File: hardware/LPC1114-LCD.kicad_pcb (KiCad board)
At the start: 2 copper layers, 80 x 76 mm, 58 parts, among them J1 USB_B_Micro, J2 SWD, J3 UART, Q1 BC337, Q2 BC337, SW1 MODE/ISP, SW2 UP, SW3 DOWN, SW4 OK, SW5 RESET, U1 LPC1114FN28/102, U2 MCP1700-3302E/TO, U3 CH340C, U4 DS3231MZ+, Y1 12MHz

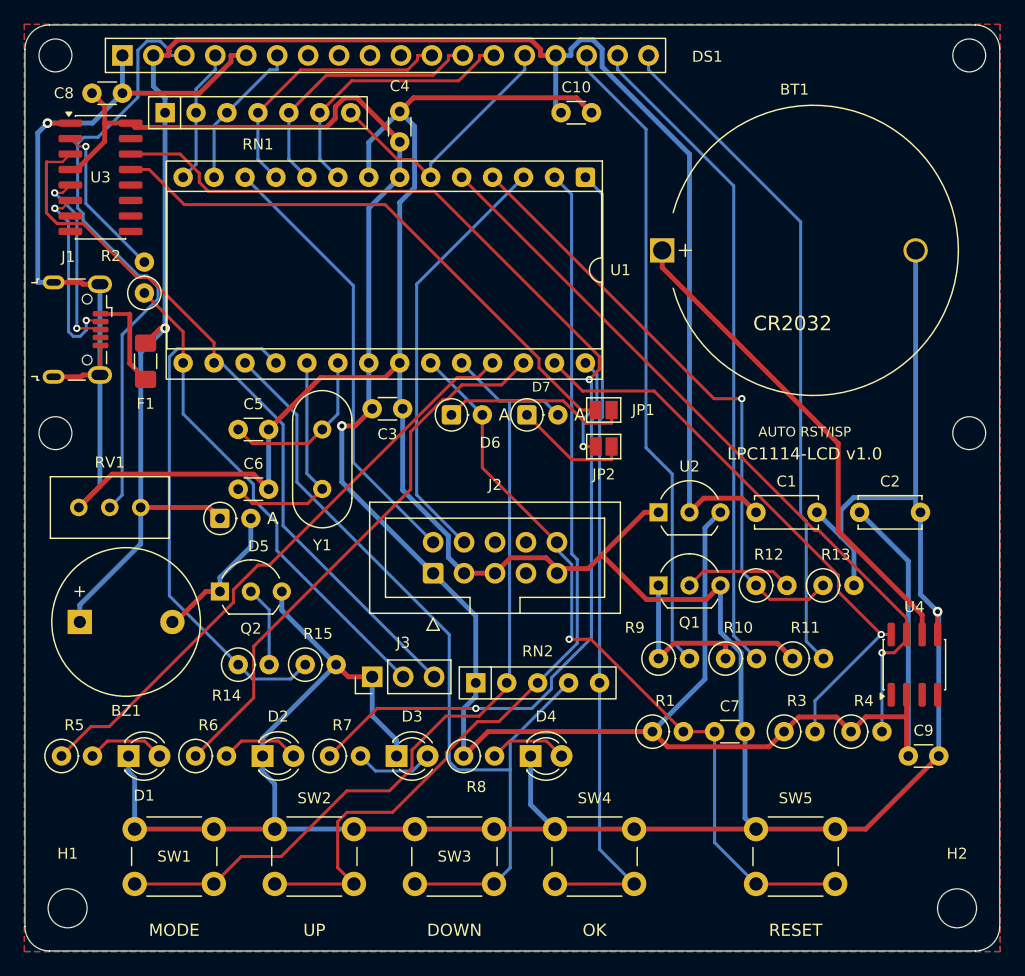
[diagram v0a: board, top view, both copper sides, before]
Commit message: Hardware v1.1: JLCPCB PCBA with Basic parts, Pomodoro timer, 80x52 mm
- Main use is now a Pomodoro timer: RTC (DS3231M) and CR2032 removed,
  timekeeping from the 12 MHz crystal; PTC fuse removed
- SMD redesign for JLCPCB assembly: 0603/0805 passives and LEDs,
  XC6206 LDO, SS8050, B5819W, 3225 crystal, TS-1187A buttons (all Basic);
  CH340C and micro USB are the only Extended parts
- User-soldered: LPC1114 (+socket), LCD, 10k multiturn trimmer,
  TDK PS1420P02CT piezo buzzer, USBLC6-2SC6, J2 (1x7 SWD+I2C) and
  J3 (1x3 UART) pads
- PCB reduced from 80x76 to 80x52 mm; ERC/DRC clean, parity OK, fully routed
- JLCPCB BOM + CPL and hand-solder list generated by export_fab.ps1
- Enclosure updated: 92.8x64.8x31.4 mm, longer button stems, LED light pipes
- Docs: schematic review for JLCPCB, design notes, README, board.h

Co-Authored-By: Claude Opus 5.5 <noreply@anthropic.com>
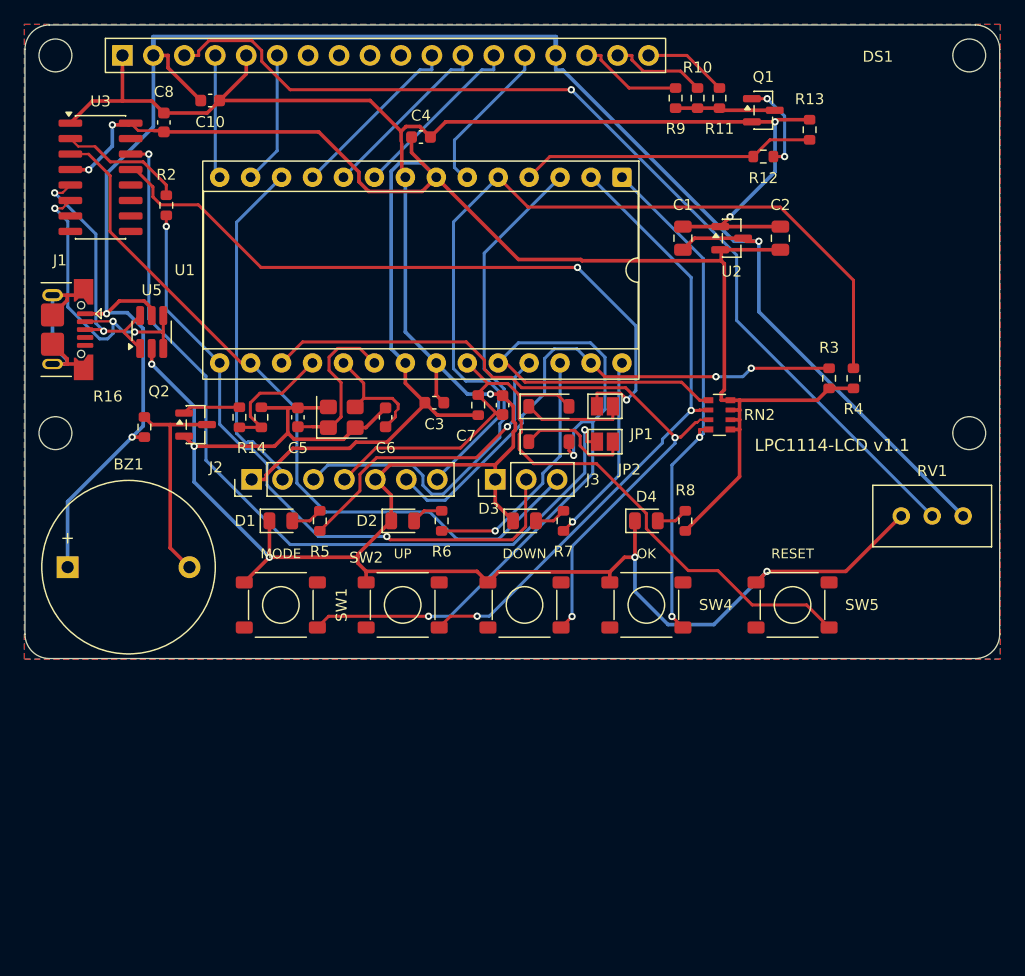
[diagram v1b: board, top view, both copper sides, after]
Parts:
- removed BT1: CR2032, Battery:BatteryHolder_MYOUNG_BS-07-A1BJ001_CR2032
- removed C9: 100nF, Capacitor_THT:C_Disc_D3.0mm_W1.6mm_P2.50mm
- removed D5: 1N4148, Diode_THT:D_DO-35_SOD27_P2.54mm_Vertical_AnodeUp
- removed F1: 500mA, Fuse:Fuse_1206_3216Metric_Pad1.42x1.75mm_HandSolder
- removed H1, H2: M3, MountingHole:MountingHole_3.2mm_M3
- removed RN1: 10k, Resistor_THT:R_Array_SIP7
- removed U4: DS3231MZ+, Package_SO:SOIC-8_3.9x4.9mm_P1.27mm
- added R16: 1k, Resistor_SMD:R_0603_1608Metric, F.Cu at (109.8, 133.0)
- added U5: USBLC6-2SC6, Package_TO_SOT_SMD:SOT-23-6_Handsoldering, F.Cu at (110.4, 125.2)
- BZ1: value Passive buzzer -> PS1420P02CT; footprint Buzzer_Beeper:Buzzer_12x9.5RM7.6 -> LPC1114-LCD:Buzzer_TDK_PS1420P02CT_D14mm_P10mm
- C1, C2: footprint Capacitor_THT:C_Disc_D5.0mm_W2.5mm_P5.00mm -> Capacitor_SMD:C_0805_2012Metric
- C10, C3, C4, C7, C8: footprint Capacitor_THT:C_Disc_D3.0mm_W1.6mm_P2.50mm -> Capacitor_SMD:C_0603_1608Metric
- C5, C6: value 18pF -> 33pF; footprint Capacitor_THT:C_Disc_D3.0mm_W1.6mm_P2.50mm -> Capacitor_SMD:C_0603_1608Metric
- D1, D2, D3, D4: footprint LED_THT:LED_D3.0mm -> LED_SMD:LED_0805_2012Metric
- D6, D7: value BAT43 -> B5819W; footprint Diode_THT:D_DO-35_SOD27_P2.54mm_Vertical_AnodeUp -> Diode_SMD:D_SOD-123
- J1: footprint Connector_USB:USB_Micro-B_Wuerth_629105150521 -> Connector_USB:USB_Micro-B_XKB_U254-051T-4BH83-F1S
- J2: value SWD -> SWD+I2C; footprint Connector_IDC:IDC-Header_2x05_P2.54mm_Vertical -> Connector_PinHeader_2.54mm:PinHeader_1x07_P2.54mm_Vertical
- Q1, Q2: value BC337 -> SS8050; footprint Package_TO_SOT_THT:TO-92_Inline_Wide -> Package_TO_SOT_SMD:SOT-23
- R1, R10, R11, R12, R13, R14, R15, R2, R3, R4, R5, R6, R7, R8, R9: footprint Resistor_THT:R_Axial_DIN0207_L6.3mm_D2.5mm_P2.54mm_Vertical -> Resistor_SMD:R_0603_1608Metric
- RN2: footprint Resistor_THT:R_Array_SIP5 -> Resistor_SMD:R_Array_Convex_4x0603
- SW1, SW2, SW3, SW4, SW5: footprint Button_Switch_THT:SW_PUSH_6mm -> LPC1114-LCD:SW_TS-1187A_5.1x5.1mm
- U2: value MCP1700-3302E/TO -> XC6206P332MR-G; footprint Package_TO_SOT_THT:TO-92_Inline_Wide -> Package_TO_SOT_SMD:SOT-23
- Y1: footprint Crystal:Crystal_HC49-4H_Vertical -> Crystal:Crystal_SMD_3225-4Pin_3.2x2.5mm
- moved RV1 67.5 mm to (177.0, 140.3)
- moved R11 46.4 mm to (157.0, 106.0), turned to 90 degrees
- moved R10 46.1 mm to (155.2, 106.0), turned to 90 degrees
- moved R9 46.0 mm to (153.4, 106.0), turned to 90 degrees
- moved Q1 39.9 mm to (160.6, 107.0)
- moved R13 37.4 mm to (164.4, 108.6), turned to 90 degrees
- moved R12 35.2 mm to (160.6, 110.8)
- moved C7 32.0 mm to (139.2, 131.2), turned to 90 degrees
- moved R1 30.4 mm to (137.2, 131.2), turned to 90 degrees
- moved RN2 29.7 mm to (157.0, 132.0)
- moved R3 29.2 mm to (166.0, 129.0), turned to 90 degrees
- moved R4 29.0 mm to (168.0, 129.0), turned to 90 degrees
- moved C10 28.8 mm to (115.2, 106.2)
- moved R5 28.7 mm to (124.2, 140.7), turned to 90 degrees
- moved R6 27.9 mm to (134.2, 140.7), turned to 90 degrees
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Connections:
- J1 pad 1: /VBUS -> +5V
- J2 pad 3: GND -> /SWCLK
- J2 pad 4: /SWCLK -> /nRESET
- J2 pad 6: unconnected-(J2-SWO/TDO-Pad6) -> /I2C_SCL
- J2 pad 7: unconnected-(J2-KEY-Pad7) -> /I2C_SDA
- Q1 pad 1: /LCD_K -> Net-(Q1-B)
- Q1 pad 2: Net-(Q1-B) -> GND
- Q1 pad 3: GND -> /LCD_K
- Q2 pad 1: /BUZ_K -> Net-(Q2-B)
- Q2 pad 2: Net-(Q2-B) -> GND
- Q2 pad 3: GND -> /BUZ_K
- RN2 pad 1: +3V3 -> /BTN_MODE
- RN2 pad 2: /BTN_MODE -> /BTN_UP
- RN2 pad 3: /BTN_UP -> /BTN_DOWN
- RN2 pad 4: /BTN_DOWN -> /BTN_OK
- RN2 pad 5: /BTN_OK -> +3V3
- U2 pad 2: +5V -> +3V3
- U2 pad 3: +3V3 -> +5V
- Y1 pad 2: /XTAL_OUT -> GND
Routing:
- net GND: track 395.9 -> 289.6 mm, vias 2 -> 8
- net /LCD_P18: track 55.4 -> 6.93 mm
- net /LCD_P17: track 54.2 -> 7.90 mm
- net /LCD_P16: track 53.0 -> 8.62 mm
- net /VBAT: track 40.4 -> 0.00 mm
- net /LED3: track 49.2 -> 15.8 mm
- net /BUZZER: track 43.6 -> 10.6 mm
- net /LCD_V0: track 49.8 -> 81.9 mm, vias 0 -> 1
- net /LCD_BL: track 50.2 -> 24.3 mm, vias 1 -> 0
- net /LED2: track 45.5 -> 20.4 mm, vias 0 -> 1
- net /BTN_UP: track 77.2 -> 52.2 mm, vias 0 -> 2
- net +3V3: track 180.7 -> 156.4 mm, vias 1 -> 2
- net /BTN_OK: track 66.4 -> 42.5 mm, vias 0 -> 2
- net /LED1: track 49.4 -> 25.7 mm, vias 0 -> 1
- net /CH340_RTS: track 54.9 -> 70.4 mm
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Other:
- board size 80 x 76 mm -> 80 x 52 mm
- board text added: "J2: 3V3 SWDIO SWCLK RST GND SCL SDA"
- board text added: "J3 UART: 1=GND 2=RX(in) 3=TX(out) 3.3V"
- board text added: "LPC1114-LCD Rev 1.1 (2026-09)"
- board text added: "LPC1114-LCD v1.1"
- board text added: "Pomodoro timer: LPC1114FN28 + LCD1602 + CH340C"
- board text removed: "AUTO RST/ISP"
- board text removed: "CR2032"
- board text removed: "J2 SWD: ARM Cortex 10-pin 2.54mm"
- board text removed: "J3 UART: 1=GND 2=RX(in) 3=TX(out) 3V3"
- board text removed: "LPC1114-LCD Rev 1.0 (2026-09)"
- board text removed: "LPC1114-LCD v1.0"
- board text removed: "LPC1114FN28 + LCD1602 + DS3231M + CH340C"

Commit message: Hardware v1.2: optional RTC (DNP), USBLC6 bypass and UART source selection
- Optional RTC on the bottom side, marked DNP: DS3231MZ+ (U4) between the
  DIP rows, C9 and a Keystone 3034 SMD CR2032 holder (BT1) on the J2 I2C bus;
  excluded from the JLCPCB BOM/CPL, listed in LPC1114-LCD_DNP_options.csv
- USB D+/D- now flow through U5 (USBLC6-2SC6); JP3/JP4 (bottom, open)
  bypass it when U5 is not fitted
- UART source selection: JP5/JP6 3-pad jumpers (bottom), 1-2 CH340
  (bridged by default), 2-3 external UART on J3, so both never connect together
- ERC/DRC clean, schematic parity OK (DNP attributes), fully connected
- Enclosure: 1 mm base pocket for the optional battery holder
- Docs: jumper configuration table, design notes, README, board.h

Co-Authored-By: Claude Opus 5.5 <noreply@anthropic.com>
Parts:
- added BT1: CR2032, Battery:BatteryHolder_Keystone_3034_1x20mm, B.Cu at (165.5, 118.5)
- added C9: 100nF, Capacitor_SMD:C_0603_1608Metric, B.Cu at (137.4, 120.1)
- added JP3: BYP_D+, Jumper:SolderJumper-2_P1.3mm_Open_Pad1.0x1.5mm, B.Cu at (111.0, 121.6)
- added JP4: BYP_D-, Jumper:SolderJumper-2_P1.3mm_Open_Pad1.0x1.5mm, B.Cu at (111.0, 129.0)
- added JP5: RX_SEL, Jumper:SolderJumper-3_P1.3mm_Bridged12_Pad1.0x1.5mm, B.Cu at (116.5, 131.6)
- added JP6: TX_SEL, Jumper:SolderJumper-3_P1.3mm_Bridged12_Pad1.0x1.5mm, B.Cu at (116.5, 134.6)
- added U4: DS3231MZ+, Package_SO:SOIC-8_3.9x4.9mm_P1.27mm, B.Cu at (132.0, 120.1)
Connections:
- J1 pad 2: /USB_DM -> /USB_DM_C
- J1 pad 3: /USB_DP -> /USB_DP_C
- J3 pad 2: /UART_RXD -> /EXT_RXD
- J3 pad 3: /UART_TXD -> /EXT_TXD
- R2 pad 1: /UART_RXD -> /CH340_TXD_R
- U3 pad 3: /UART_TXD -> /CH340_RXD
- U5 pad 1: /USB_DP -> /USB_DP_C
- U5 pad 3: /USB_DM -> /USB_DM_C
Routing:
- net /VBAT: track 0.00 -> 56.4 mm, vias 0 -> 4
- net /UART_TXD: track 61.4 -> 8.48 mm
- net /UART_RXD: track 53.4 -> 4.08 mm, vias 2 -> 0
- net /EXT_RXD: track 0.00 -> 37.2 mm
- net /CH340_RXD: track 0.00 -> 34.9 mm, vias 0 -> 1
- net /EXT_TXD: track 0.00 -> 34.9 mm, vias 0 -> 1
- net GND: track 289.6 -> 320.7 mm, vias 8 -> 4
- net /I2C_SCL: track 43.8 -> 64.6 mm, vias 2 -> 5
- net /CH340_TXD_R: track 0.00 -> 19.0 mm, vias 0 -> 1
- net /BTN_MODE: track 71.5 -> 56.1 mm, vias 2 -> 3
- net /USB_DM_C: track 0.00 -> 12.1 mm, vias 0 -> 1
- net /CH340_RTS: track 70.4 -> 58.2 mm
- net /USB_DP_C: track 0.00 -> 10.6 mm, vias 0 -> 1
- net /I2C_SDA: track 70.9 -> 77.7 mm, vias 0 -> 1
- net /CH340_DTR: track 57.4 -> 51.1 mm
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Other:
- board text added: "JP3/JP4: bridge if U5 not fitted"
- board text added: "JP5/JP6: 1-2 CH340 (default) 2-3 J3"
- board text added: "LPC1114-LCD Rev 1.2 (2026-09)"
- board text added: "LPC1114-LCD v1.2"
- board text added: "RTC U4/C9/BT1: optional (DNP)"
- board text removed: "LPC1114-LCD Rev 1.1 (2026-09)"
- board text removed: "LPC1114-LCD v1.1"
